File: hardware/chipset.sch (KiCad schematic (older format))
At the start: 1 part

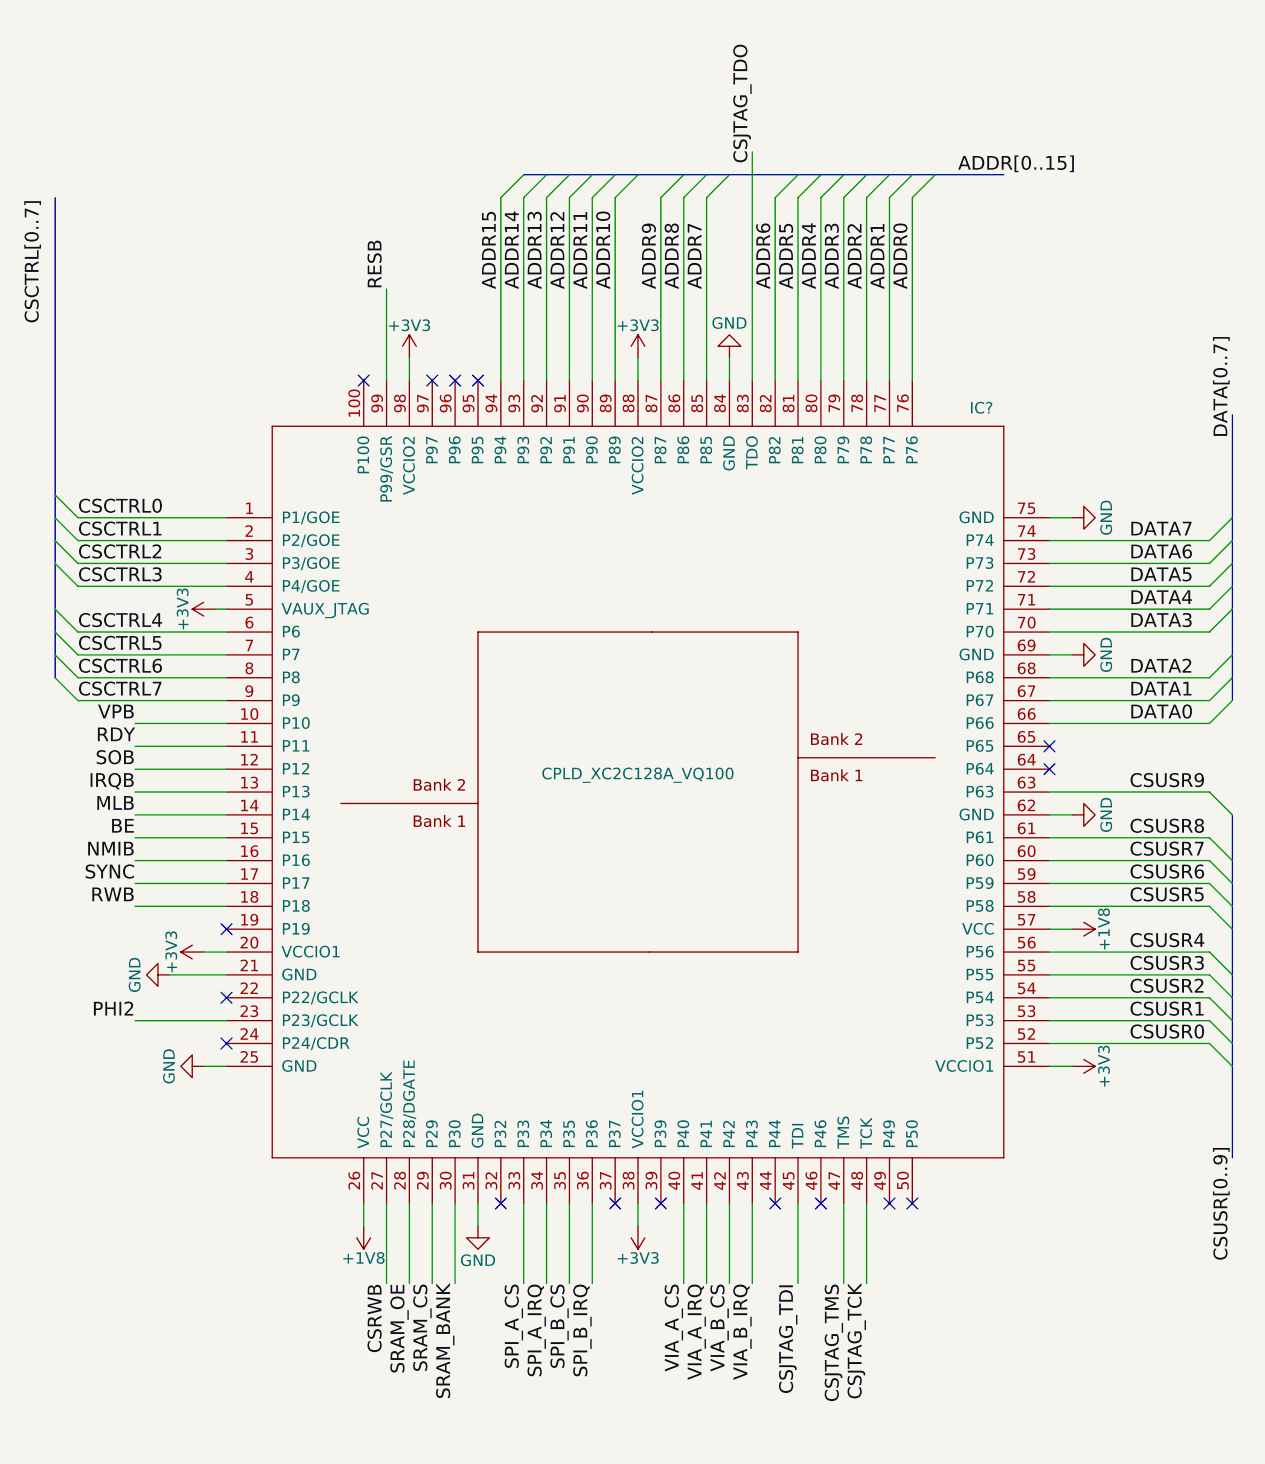
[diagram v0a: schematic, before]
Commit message: hardware: chipset hierarchical pins
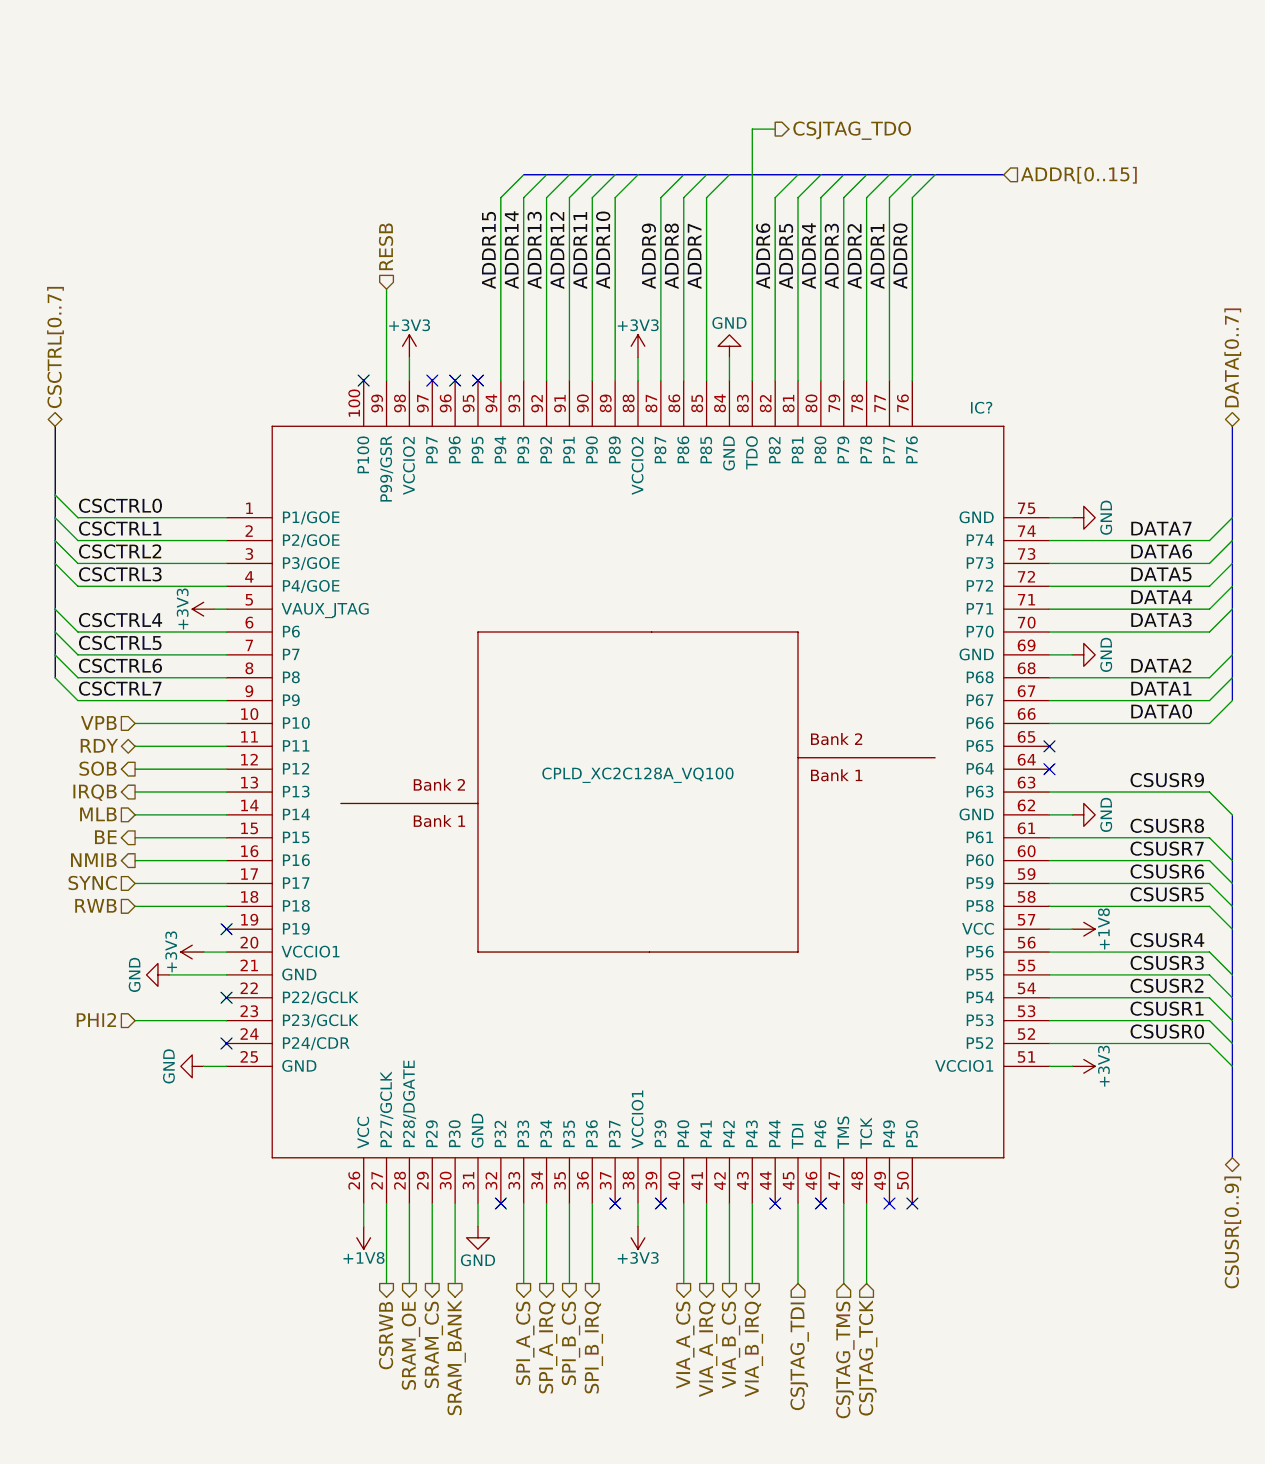
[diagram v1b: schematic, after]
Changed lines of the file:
@@
 $EndComp
 $Comp
-L GND #PWR?
+L GND #PWR01
 U 1 1 58EB9275
 P 2150 5200
-F 0 "#PWR?" H 2150 4950 50  0001 C CNN
+F 0 "#PWR01" H 2150 4950 50  0001 C CNN
 F 1 "GND" H 2150 5050 50  0000 C CNN
 F 2 "" H 2150 5200 50  0001 C CNN
@@
 $EndComp
 $Comp
-L GND #PWR?
+L GND #PWR02
 U 1 1 58EB92A0
 P 3350 5900
-F 0 "#PWR?" H 3350 5650 50  0001 C CNN
+F 0 "#PWR02" H 3350 5650 50  0001 C CNN
 F 1 "GND" H 3350 5750 50  0000 C CNN
 F 2 "" H 3350 5900 50  0001 C CNN
@@
 $EndComp
 $Comp
-L +1V8 #PWR?
+L +1V8 #PWR03
 U 1 1 58EB92FD
 P 2850 5900
-F 0 "#PWR?" H 2850 5750 50  0001 C CNN
+F 0 "#PWR03" H 2850 5750 50  0001 C CNN
 F 1 "+1V8" H 2850 6040 50  0000 C CNN
 F 2 "" H 2850 5900 50  0001 C CNN
@@
 $EndComp
 $Comp
-L +1V8 #PWR?
+L +1V8 #PWR04
 U 1 1 58EB9325
 P 5950 4600
-F 0 "#PWR?" H 5950 4450 50  0001 C CNN
+F 0 "#PWR04" H 5950 4450 50  0001 C CNN
 F 1 "+1V8" H 5950 4740 50  0000 C CNN
 F 2 "" H 5950 4600 50  0001 C CNN
@@
 $EndComp
 $Comp
-L +3V3 #PWR?
+L +3V3 #PWR05
 U 1 1 58EB9443
 P 3050 2100
-F 0 "#PWR?" H 3050 1950 50  0001 C CNN
+F 0 "#PWR05" H 3050 1950 50  0001 C CNN
 F 1 "+3V3" H 3050 2240 50  0000 C CNN
 F 2 "" H 3050 2100 50  0001 C CNN
@@
 $EndComp
 $Comp
-L +3V3 #PWR?
+L +3V3 #PWR06
 U 1 1 58EB9457
 P 4050 2100
-F 0 "#PWR?" H 4050 1950 50  0001 C CNN
+F 0 "#PWR06" H 4050 1950 50  0001 C CNN
 F 1 "+3V3" H 4050 2240 50  0000 C CNN
 F 2 "" H 4050 2100 50  0001 C CNN
@@
 $EndComp
 $Comp
-L +3V3 #PWR?
+L +3V3 #PWR07
 U 1 1 58EB9469
 P 2150 4700
-F 0 "#PWR?" H 2150 4550 50  0001 C CNN
+F 0 "#PWR07" H 2150 4550 50  0001 C CNN
 F 1 "+3V3" H 2150 4840 50  0000 C CNN
 F 2 "" H 2150 4700 50  0001 C CNN
@@
 $EndComp
 $Comp
-L +3V3 #PWR?
+L +3V3 #PWR08
 U 1 1 58EB947B
 P 2200 3200
-F 0 "#PWR?" H 2200 3050 50  0001 C CNN
+F 0 "#PWR08" H 2200 3050 50  0001 C CNN
 F 1 "+3V3" H 2200 3340 50  0000 C CNN
 F 2 "" H 2200 3200 50  0001 C CNN
@@
 $EndComp
 $Comp
-L +3V3 #PWR?
+L +3V3 #PWR09
 U 1 1 58EB948D
 P 4050 5900
-F 0 "#PWR?" H 4050 5750 50  0001 C CNN
+F 0 "#PWR09" H 4050 5750 50  0001 C CNN
 F 1 "+3V3" H 4050 6040 50  0000 C CNN
 F 2 "" H 4050 5900 50  0001 C CNN
@@
 $EndComp
 $Comp
-L +3V3 #PWR?
+L +3V3 #PWR010
 U 1 1 58EB949F
 P 5950 5200
-F 0 "#PWR?" H 5950 5050 50  0001 C CNN
+F 0 "#PWR010" H 5950 5050 50  0001 C CNN
 F 1 "+3V3" H 5950 5340 50  0000 C CNN
 F 2 "" H 5950 5200 50  0001 C CNN
@@
 $EndComp
 $Comp
-L GND #PWR?
+L GND #PWR011
 U 1 1 58EB957D
 P 4450 2100
-F 0 "#PWR?" H 4450 1850 50  0001 C CNN
+F 0 "#PWR011" H 4450 1850 50  0001 C CNN
 F 1 "GND" H 4450 1950 50  0000 C CNN
 F 2 "" H 4450 2100 50  0001 C CNN
@@
 $EndComp
 $Comp
-L GND #PWR?
+L GND #PWR012
 U 1 1 58EB95B9
 P 5950 2800
-F 0 "#PWR?" H 5950 2550 50  0001 C CNN
+F 0 "#PWR012" H 5950 2550 50  0001 C CNN
 F 1 "GND" H 5950 2650 50  0000 C CNN
 F 2 "" H 5950 2800 50  0001 C CNN
@@
 $EndComp
 $Comp
-L GND #PWR?
+L GND #PWR013
 U 1 1 58EB95CD
 P 5950 3400
-F 0 "#PWR?" H 5950 3150 50  0001 C CNN
+F 0 "#PWR013" H 5950 3150 50  0001 C CNN
 F 1 "GND" H 5950 3250 50  0000 C CNN
 F 2 "" H 5950 3400 50  0001 C CNN
@@
 $EndComp
 $Comp
-L GND #PWR?
+L GND #PWR014
 U 1 1 58EB95DF
 P 5950 4100
-F 0 "#PWR?" H 5950 3850 50  0001 C CNN
+F 0 "#PWR014" H 5950 3850 50  0001 C CNN
 F 1 "GND" H 5950 3950 50  0000 C CNN
 F 2 "" H 5950 4100 50  0001 C CNN
@@
 $EndComp
 $Comp
-L GND #PWR?
+L GND #PWR015
 U 1 1 58EB9604
 P 2000 4800
-F 0 "#PWR?" H 2000 4550 50  0001 C CNN
+F 0 "#PWR015" H 2000 4550 50  0001 C CNN
 F 1 "GND" H 2000 4650 50  0000 C CNN
 F 2 "" H 2000 4800 50  0001 C CNN
@@
 	0    1    1    0
 $EndComp
-Text Label 5450 1300 0    60   ~ 0
-ADDR[0..15]
-Text Label 6650 2450 1    60   ~ 0
-DATA[0..7]
 Text Label 6200 2900 0    60   ~ 0
 DATA7
@@
 Text Label 3450 1800 1    60   ~ 0
 ADDR15
-Text Label 1850 4500 2    60   ~ 0
-RWB
-Text Label 1850 5000 2    60   ~ 0
-PHI2
-Text Label 2950 1800 1    60   ~ 0
-RESB
-Text Label 1850 4200 2    60   ~ 0
-BE
-Text Label 1850 4000 2    60   ~ 0
-IRQB
-Text Label 1850 4300 2    60   ~ 0
-NMIB
-Text Label 1850 4100 2    60   ~ 0
-MLB
-Text Label 1850 3800 2    60   ~ 0
-RDY
-Text Label 1850 3900 2    60   ~ 0
-SOB
-Text Label 1850 4400 2    60   ~ 0
-SYNC
-Text Label 1850 3700 2    60   ~ 0
-VPB
-Text Label 4250 6150 3    60   ~ 0
-VIA_A_CS
-Text Label 4350 6150 3    60   ~ 0
-VIA_A_IRQ
-Text Label 4450 6150 3    60   ~ 0
-VIA_B_CS
-Text Label 4550 6150 3    60   ~ 0
-VIA_B_IRQ
-Text Label 3550 6150 3    60   ~ 0
-SPI_A_CS
-Text Label 3650 6150 3    60   ~ 0
-SPI_A_IRQ
-Text Label 3750 6150 3    60   ~ 0
-SPI_B_CS
-Text Label 3850 6150 3    60   ~ 0
-SPI_B_IRQ
-Text Label 3150 6150 3    60   ~ 0
-SRAM_CS
-Text Label 3250 6150 3    60   ~ 0
-SRAM_BANK
-Text Label 6650 5550 3    60   ~ 0
-CSUSR[0..9]
-Text Label 2950 6150 3    60   ~ 0
-CSRWB
-Text Label 4550 1250 1    60   ~ 0
-CSJTAG_TDO
-Text Label 1450 1950 1    60   ~ 0
-CSCTRL[0..7]
 Text Label 1600 2800 0    60   ~ 0
 CSCTRL0
@@
 	2250 5000 1850 5000
 Wire Wire Line
-	4550 2200 4550 1200
+	4550 1100 4550 2200
 Wire Wire Line
 	2850 5800 2850 5900
@@
 	5850 4900 6550 4900
 Wire Bus Line
-	6650 2350 6650 3600
+	6650 2400 6650 3600
 Wire Bus Line
 	6650 4100 6650 5600
 Wire Bus Line
-	1500 1400 1500 3500
+	1500 2400 1500 3500
 Wire Wire Line
 	2250 3200 2200 3200
@@
 Wire Wire Line
 	3050 5800 3050 6150
-Text Label 3050 6150 3    60   ~ 0
-SRAM_OE
-Text Label 4750 6150 3    60   ~ 0
-CSJTAG_TDI
-Text Label 4950 6150 3    60   ~ 0
-CSJTAG_TMS
-Text Label 5050 6150 3    60   ~ 0
-CSJTAG_TCK
 NoConn ~ 3350 2200
 NoConn ~ 3250 2200
@@
 NoConn ~ 5850 3900
 NoConn ~ 5850 3800
+Text HLabel 5650 1300 2    60   Input ~ 0
+ADDR[0..15]
+Text HLabel 1500 2400 1    60   BiDi ~ 0
+CSCTRL[0..7]
+Text HLabel 6650 5600 3    60   BiDi ~ 0
+CSUSR[0..9]
+Text HLabel 2950 1800 1    60   Input ~ 0
+RESB
+Text HLabel 1850 3700 0    60   Input ~ 0
+VPB
+Text HLabel 1850 3800 0    60   BiDi ~ 0
+RDY
+Text HLabel 1850 3900 0    60   Output ~ 0
+SOB
+Text HLabel 1850 4000 0    60   Output ~ 0
+IRQB
+Text HLabel 1850 4100 0    60   Input ~ 0
+MLB
+Text HLabel 1850 4200 0    60   Output ~ 0
+BE
+Text HLabel 1850 4300 0    60   Output ~ 0
+NMIB
+Text HLabel 1850 4400 0    60   Input ~ 0
+SYNC
+Text HLabel 1850 4500 0    60   Input ~ 0
+RWB
+Text HLabel 1850 5000 0    60   Input ~ 0
+PHI2
+Text HLabel 2950 6150 3    60   Output ~ 0
+CSRWB
+Text HLabel 3050 6150 3    60   Output ~ 0
+SRAM_OE
+Text HLabel 3150 6150 3    60   Output ~ 0
+SRAM_CS
+Text HLabel 3250 6150 3    60   Output ~ 0
+SRAM_BANK
+Text HLabel 3550 6150 3    60   Output ~ 0
+SPI_A_CS
+Text HLabel 3650 6150 3    60   Output ~ 0
+SPI_A_IRQ
+Text HLabel 3750 6150 3    60   Output ~ 0
+SPI_B_CS
+Text HLabel 3850 6150 3    60   Output ~ 0
+SPI_B_IRQ
+Text HLabel 4250 6150 3    60   Output ~ 0
+VIA_A_CS
+Text HLabel 4350 6150 3    60   Output ~ 0
+VIA_A_IRQ
+Text HLabel 4450 6150 3    60   Output ~ 0
+VIA_B_CS
+Text HLabel 4550 6150 3    60   Output ~ 0
+VIA_B_IRQ
+Text HLabel 4750 6150 3    60   Input ~ 0
+CSJTAG_TDI
+Text HLabel 4950 6150 3    60   Input ~ 0
+CSJTAG_TMS
+Text HLabel 5050 6150 3    60   Input ~ 0
+CSJTAG_TCK
+Text HLabel 4650 1100 2    60   Output ~ 0
+CSJTAG_TDO
+Text HLabel 6650 2400 1    60   BiDi ~ 0
+DATA[0..7]
+Wire Wire Line
+	4550 1100 4650 1100
 $EndSCHEMATC

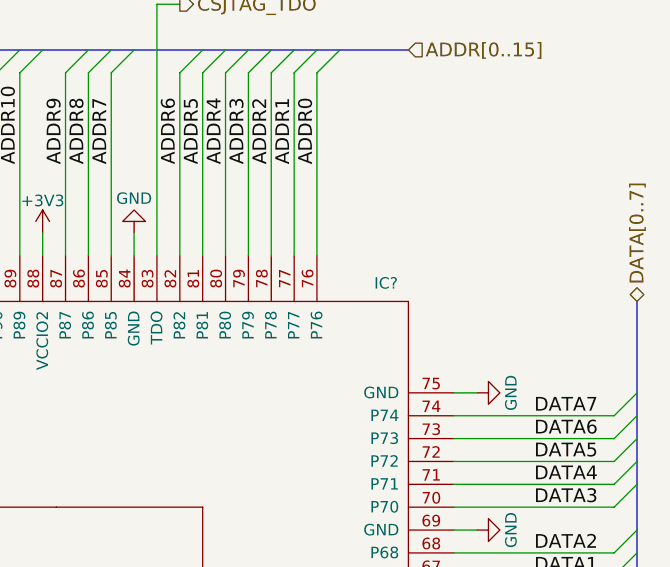
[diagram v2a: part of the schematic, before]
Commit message: hardware: schematic for 2 x 6522 VIA/GPIO.
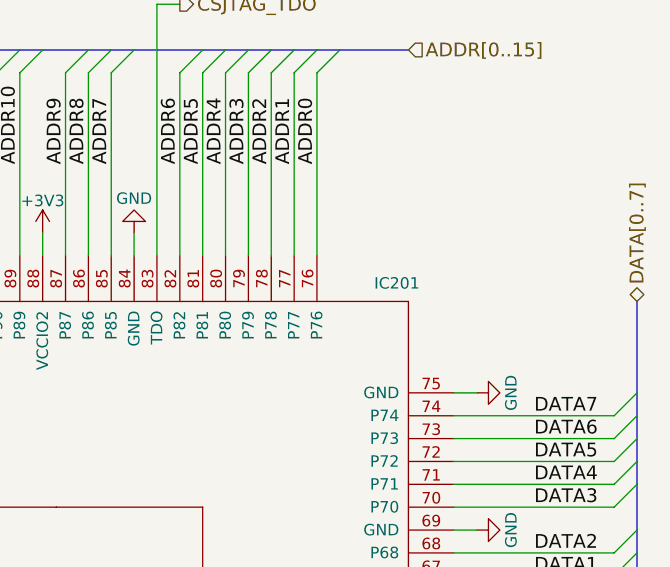
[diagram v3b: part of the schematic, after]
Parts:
- gave numbers to parts that had none: 1
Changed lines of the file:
@@
 $Descr A4 11693 8268
 encoding utf-8
-Sheet 2 3
+Sheet 2 5
 Title "pda6502v2: CPLD chipset"
 Date ""
@@
 $EndDescr
 $Comp
-L CPLD_XC2C128A_VQ100 IC?
+L CPLD_XC2C128A_VQ100 IC201
 U 1 1 58EB9114
 P 4050 4000
-F 0 "IC?" H 5500 5650 50  0000 L BNN
+F 0 "IC201" H 5500 5650 50  0000 L BNN
 F 1 "CPLD_XC2C128A_VQ100" H 4050 4050 50  0000 C BNN
 F 2 "VQ-100" H 4050 3900 50  0001 C CNN
@@
 $EndComp
 $Comp
-L GND #PWR01
+L GND #PWR203
 U 1 1 58EB9275
 P 2150 5200
-F 0 "#PWR01" H 2150 4950 50  0001 C CNN
+F 0 "#PWR203" H 2150 4950 50  0001 C CNN
 F 1 "GND" H 2150 5050 50  0000 C CNN
 F 2 "" H 2150 5200 50  0001 C CNN
@@
 $EndComp
 $Comp
-L GND #PWR02
+L GND #PWR207
 U 1 1 58EB92A0
 P 3350 5900
-F 0 "#PWR02" H 3350 5650 50  0001 C CNN
+F 0 "#PWR207" H 3350 5650 50  0001 C CNN
 F 1 "GND" H 3350 5750 50  0000 C CNN
 F 2 "" H 3350 5900 50  0001 C CNN
@@
 $EndComp
 $Comp
-L +1V8 #PWR03
+L +1V8 #PWR205
 U 1 1 58EB92FD
 P 2850 5900
-F 0 "#PWR03" H 2850 5750 50  0001 C CNN
+F 0 "#PWR205" H 2850 5750 50  0001 C CNN
 F 1 "+1V8" H 2850 6040 50  0000 C CNN
 F 2 "" H 2850 5900 50  0001 C CNN
@@
 $EndComp
 $Comp
-L +1V8 #PWR04
+L +1V8 #PWR214
 U 1 1 58EB9325
 P 5950 4600
-F 0 "#PWR04" H 5950 4450 50  0001 C CNN
+F 0 "#PWR214" H 5950 4450 50  0001 C CNN
 F 1 "+1V8" H 5950 4740 50  0000 C CNN
 F 2 "" H 5950 4600 50  0001 C CNN
@@
 $EndComp
 $Comp
-L +3V3 #PWR05
+L +3V3 #PWR206
 U 1 1 58EB9443
 P 3050 2100
-F 0 "#PWR05" H 3050 1950 50  0001 C CNN
+F 0 "#PWR206" H 3050 1950 50  0001 C CNN
 F 1 "+3V3" H 3050 2240 50  0000 C CNN
 F 2 "" H 3050 2100 50  0001 C CNN
@@
 $EndComp
 $Comp
-L +3V3 #PWR06
+L +3V3 #PWR208
 U 1 1 58EB9457
 P 4050 2100
-F 0 "#PWR06" H 4050 1950 50  0001 C CNN
+F 0 "#PWR208" H 4050 1950 50  0001 C CNN
 F 1 "+3V3" H 4050 2240 50  0000 C CNN
 F 2 "" H 4050 2100 50  0001 C CNN
@@
 $EndComp
 $Comp
-L +3V3 #PWR07
+L +3V3 #PWR202
 U 1 1 58EB9469
 P 2150 4700
-F 0 "#PWR07" H 2150 4550 50  0001 C CNN
+F 0 "#PWR202" H 2150 4550 50  0001 C CNN
 F 1 "+3V3" H 2150 4840 50  0000 C CNN
 F 2 "" H 2150 4700 50  0001 C CNN
@@
 $EndComp
 $Comp
-L +3V3 #PWR08
+L +3V3 #PWR204
 U 1 1 58EB947B
 P 2200 3200
-F 0 "#PWR08" H 2200 3050 50  0001 C CNN
+F 0 "#PWR204" H 2200 3050 50  0001 C CNN
 F 1 "+3V3" H 2200 3340 50  0000 C CNN
 F 2 "" H 2200 3200 50  0001 C CNN
@@
 $EndComp
 $Comp
-L +3V3 #PWR09
+L +3V3 #PWR209
 U 1 1 58EB948D
 P 4050 5900
-F 0 "#PWR09" H 4050 5750 50  0001 C CNN
+F 0 "#PWR209" H 4050 5750 50  0001 C CNN
 F 1 "+3V3" H 4050 6040 50  0000 C CNN
 F 2 "" H 4050 5900 50  0001 C CNN
@@
 $EndComp
 $Comp
-L +3V3 #PWR010
+L +3V3 #PWR215
 U 1 1 58EB949F
 P 5950 5200
-F 0 "#PWR010" H 5950 5050 50  0001 C CNN
+F 0 "#PWR215" H 5950 5050 50  0001 C CNN
 F 1 "+3V3" H 5950 5340 50  0000 C CNN
 F 2 "" H 5950 5200 50  0001 C CNN
@@
 $EndComp
 $Comp
-L GND #PWR011
+L GND #PWR210
 U 1 1 58EB957D
 P 4450 2100
-F 0 "#PWR011" H 4450 1850 50  0001 C CNN
+F 0 "#PWR210" H 4450 1850 50  0001 C CNN
 F 1 "GND" H 4450 1950 50  0000 C CNN
 F 2 "" H 4450 2100 50  0001 C CNN
@@
 $EndComp
 $Comp
-L GND #PWR012
+L GND #PWR211
 U 1 1 58EB95B9
 P 5950 2800
-F 0 "#PWR012" H 5950 2550 50  0001 C CNN
+F 0 "#PWR211" H 5950 2550 50  0001 C CNN
 F 1 "GND" H 5950 2650 50  0000 C CNN
 F 2 "" H 5950 2800 50  0001 C CNN
@@
 $EndComp
 $Comp
-L GND #PWR013
+L GND #PWR212
 U 1 1 58EB95CD
 P 5950 3400
-F 0 "#PWR013" H 5950 3150 50  0001 C CNN
+F 0 "#PWR212" H 5950 3150 50  0001 C CNN
 F 1 "GND" H 5950 3250 50  0000 C CNN
 F 2 "" H 5950 3400 50  0001 C CNN
@@
 $EndComp
 $Comp
-L GND #PWR014
+L GND #PWR213
 U 1 1 58EB95DF
 P 5950 4100
-F 0 "#PWR014" H 5950 3850 50  0001 C CNN
+F 0 "#PWR213" H 5950 3850 50  0001 C CNN
 F 1 "GND" H 5950 3950 50  0000 C CNN
 F 2 "" H 5950 4100 50  0001 C CNN
@@
 $EndComp
 $Comp
-L GND #PWR015
+L GND #PWR201
 U 1 1 58EB9604
 P 2000 4800
-F 0 "#PWR015" H 2000 4550 50  0001 C CNN
+F 0 "#PWR201" H 2000 4550 50  0001 C CNN
 F 1 "GND" H 2000 4650 50  0000 C CNN
 F 2 "" H 2000 4800 50  0001 C CNN
